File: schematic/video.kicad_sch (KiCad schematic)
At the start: 17 parts, among them J1 Conn_Coaxial, Q1 2N3904, U1 TMS4416, U14 TMS9118NL, U3 TMS4416, Y1 10.738635 MHz

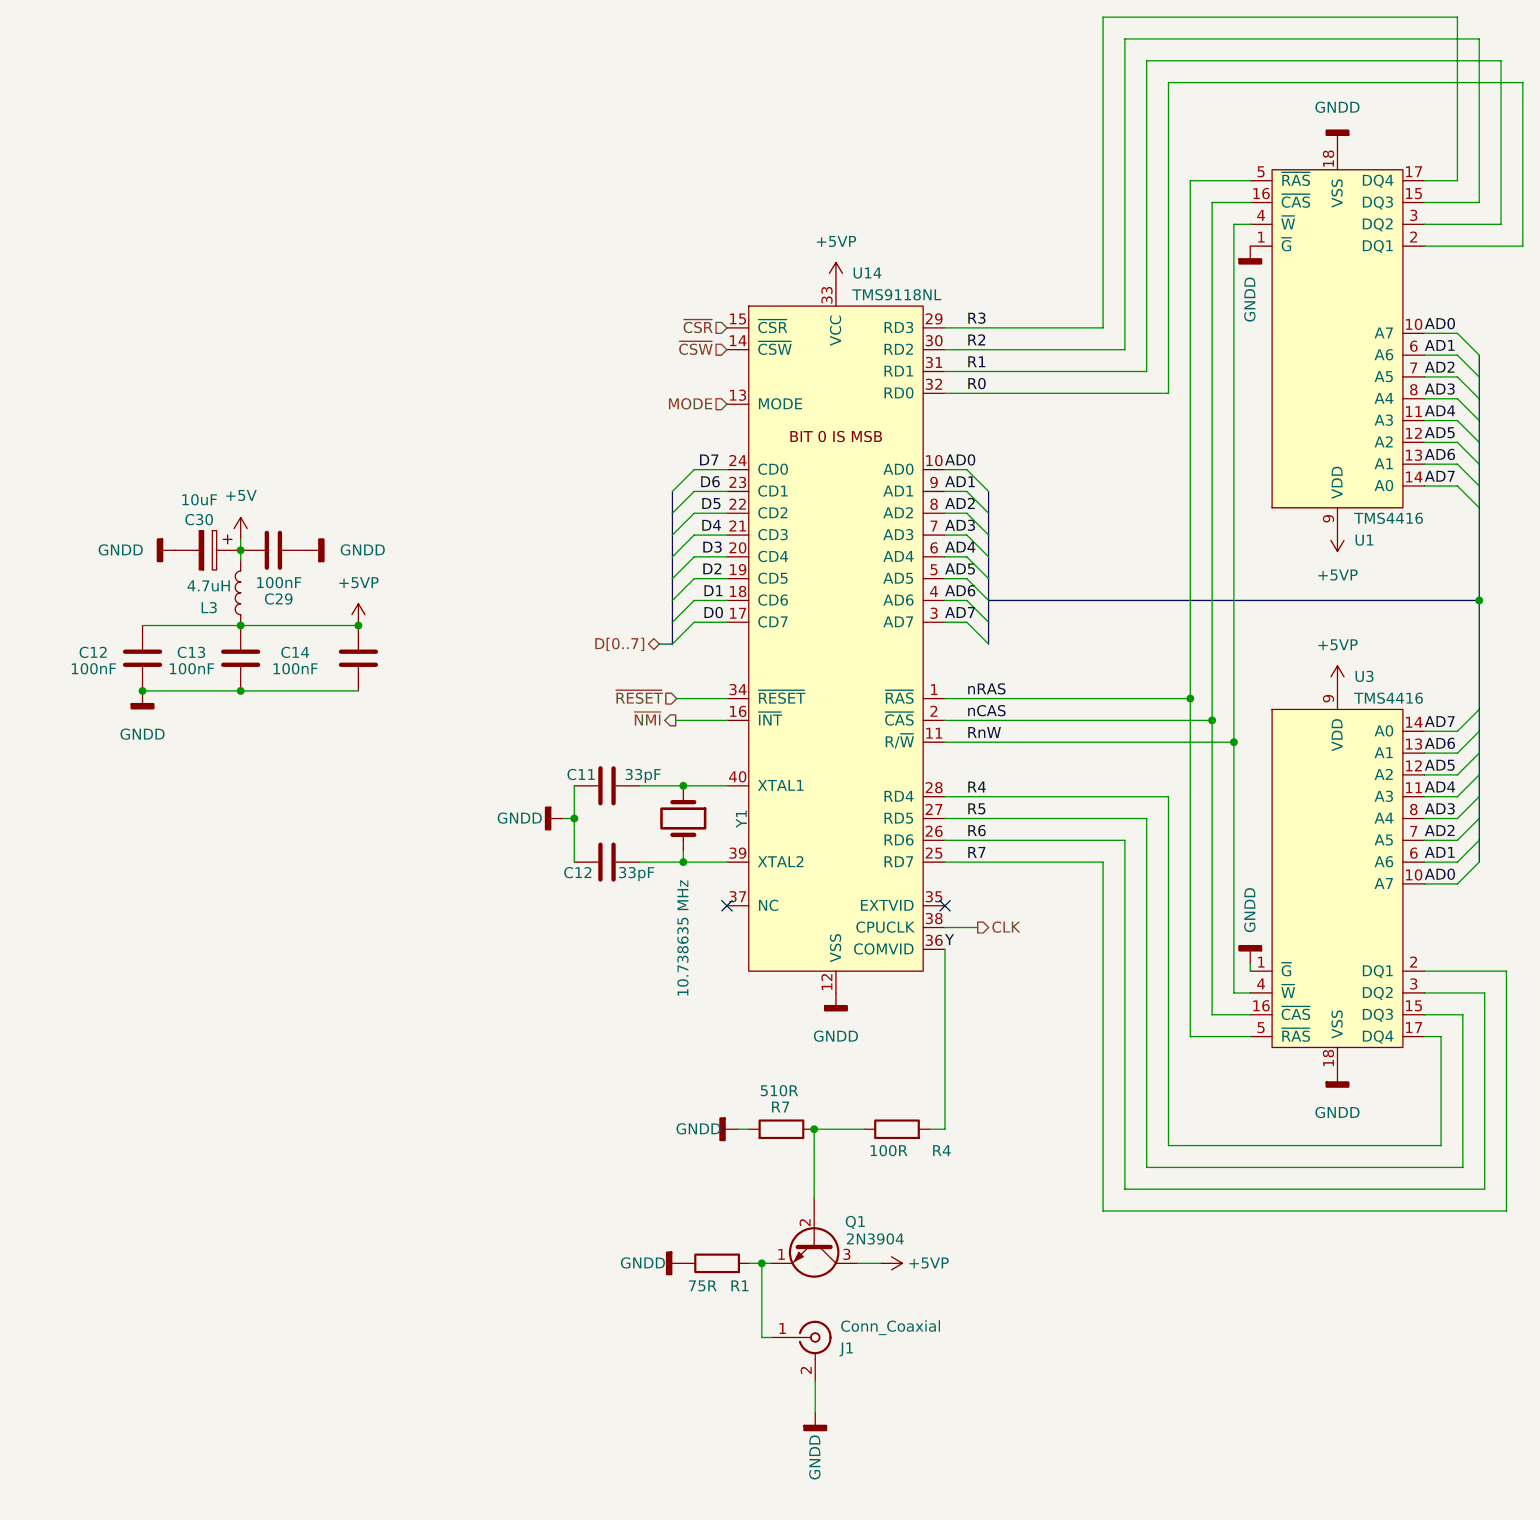
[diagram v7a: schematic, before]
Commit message: add 2 ohm resistors to pi filters for analog noise filtering
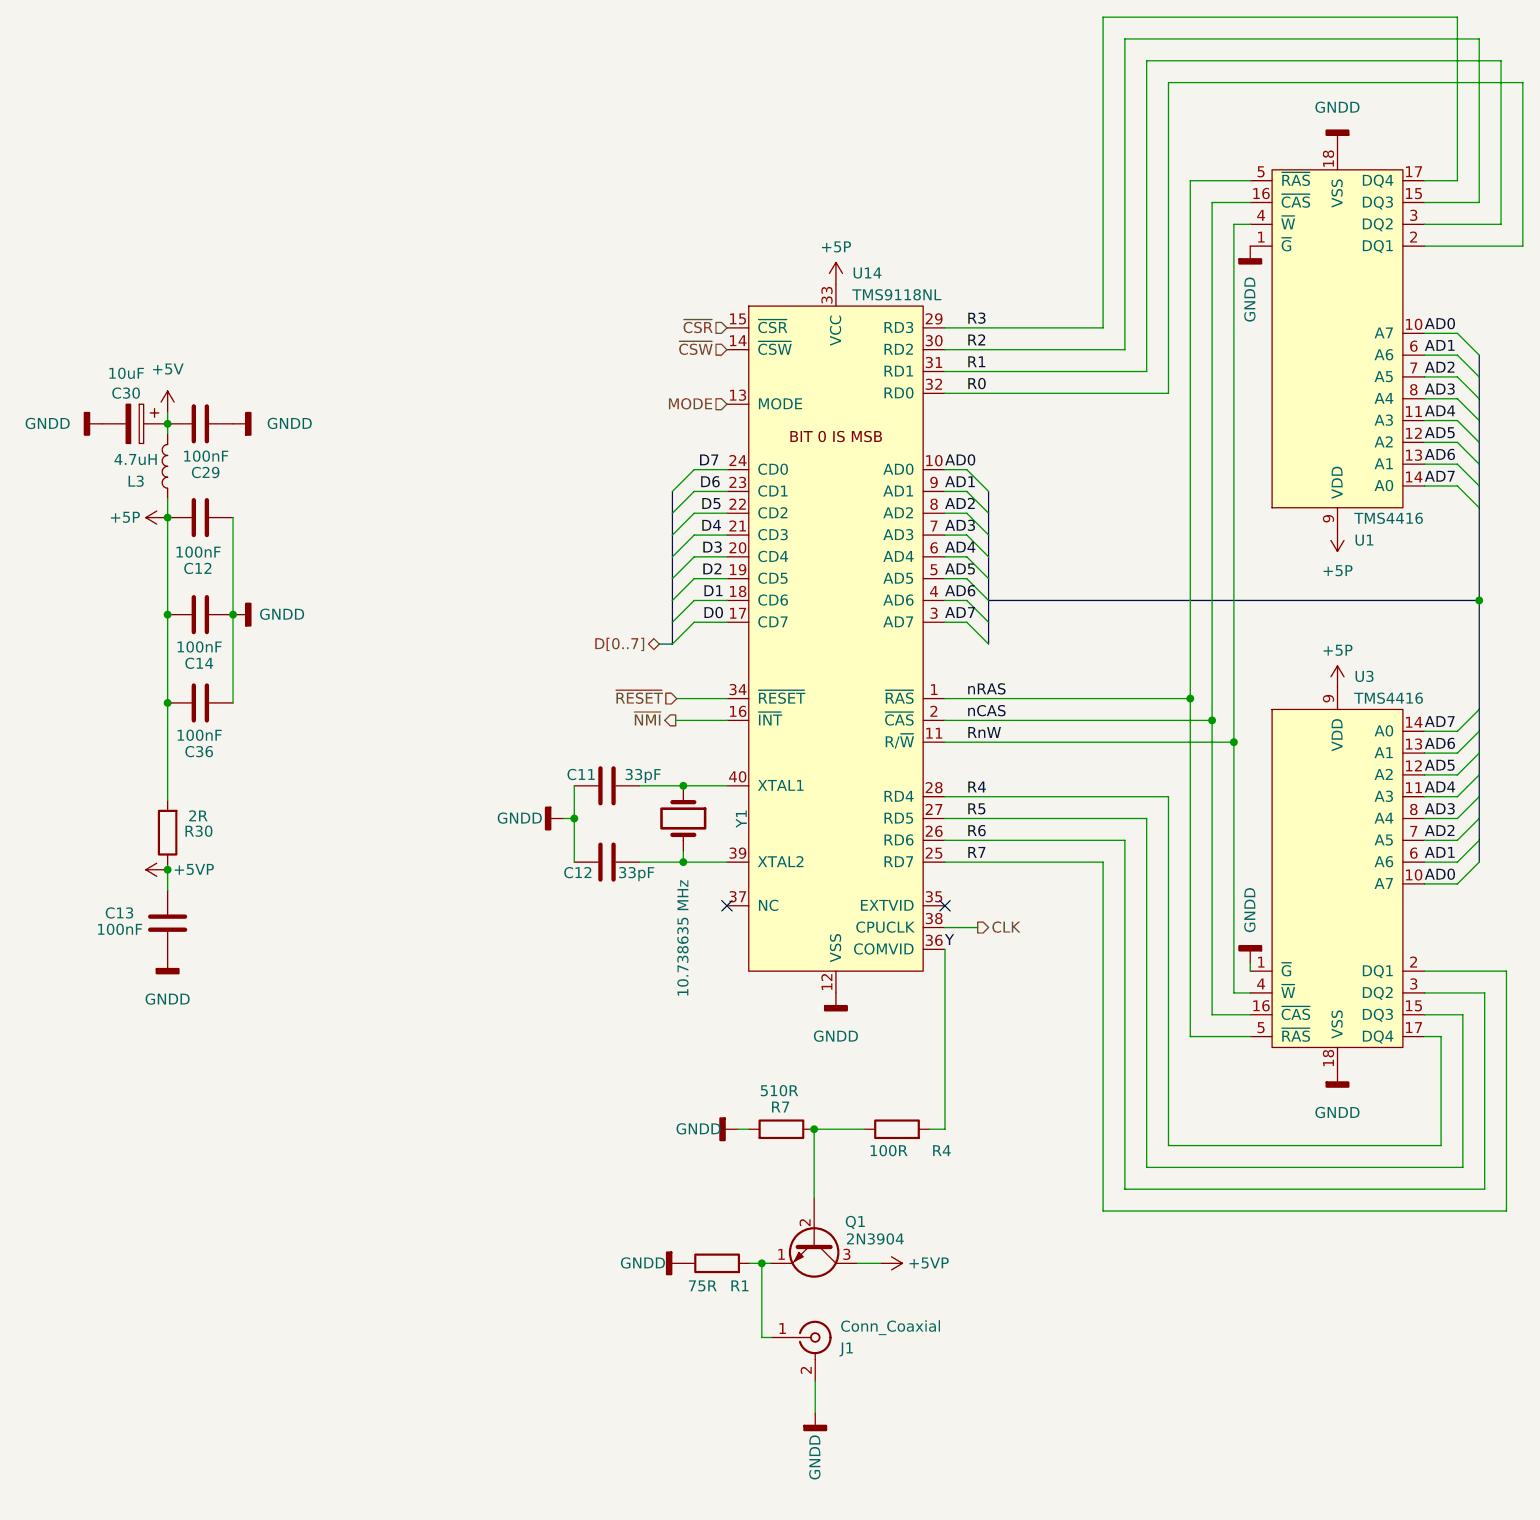
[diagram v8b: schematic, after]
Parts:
- added C36: 100nF, Capacitor_THT:C_Disc_D7.0mm_W2.5mm_P5.00mm, symbol Device:C
- added R30: 2R, Resistor_THT:R_Axial_DIN0207_L6.3mm_D2.5mm_P7.62mm_Horizontal, symbol Device:R
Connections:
- net +5VP: now also R30.1; no longer C12.1, C14.1, L3.1, U1.9 (VDD), U14.33 (VCC), U3.9 (VDD)
- net GNDD: now also C36.2
- new net +5P: C12.1, C14.1, C36.1, L3.1, R30.2, U1.9 (VDD), U14.33 (VCC), U3.9 (VDD)
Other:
- moved on the sheet: C12, C13, C14, C29, C30, L3
